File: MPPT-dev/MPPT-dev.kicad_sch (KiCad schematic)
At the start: 0 parts

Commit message: basic mppt
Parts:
- added U1: STM32L412KBUx, Package_DFN_QFN:QFN-32-1EP_5x5mm_P0.5mm_EP3.45x3.45mm, symbol MCU_ST_STM32L4:STM32L412KBUx
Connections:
- new net: U1.16 (VSS), U1.32 (VSS), U1.33 (VSS)
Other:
- added sheet MPPT (untitled.kicad_sch)
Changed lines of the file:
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@@
 	(generator_version "9.0")
 	(paper "A4")
+	(label "SDA"
+		(at 86.36 91.44 0)
+		(effects
+			(font
+				(size 1.27 1.27)
+			)
+			(justify left bottom)
+		)
+	)
+	(label "SCL"
+		(at 86.36 82.55 0)
+		(effects
+			(font
+				(size 1.27 1.27)
+			)
+			(justify left bottom)
+		)
+	)
+	(symbol
+		(lib_id "MCU_ST_STM32L4:STM32L412KBUx")
+		(at 69.85 92.71 0)
+		(unit 1)
+		(exclude_from_sim no)
+		(in_bom yes)
+		(on_board yes)
+		(dnp no)
+		(fields_autoplaced yes)
+		(property "Reference" "U1"
+			(at 71.9933 118.11 0)
+			(effects
+				(font
+					(size 1.27 1.27)
+				)
+				(justify left)
+			)
+		)
+		(property "Value" "STM32L412KBUx"
+			(at 71.9933 120.65 0)
+			(effects
+				(font
+					(size 1.27 1.27)
+				)
+				(justify left)
+			)
+		)
+		(property "Footprint" "Package_DFN_QFN:QFN-32-1EP_5x5mm_P0.5mm_EP3.45x3.45mm"
+			(at 59.69 115.57 0)
+			(effects
+				(font
+					(size 1.27 1.27)
+				)
+				(justify right)
+				(hide yes)
+			)
+		)
+		(property "Datasheet" "https://www.st.com/resource/en/datasheet/stm32l412kb.pdf"
+			(at 69.85 92.71 0)
+			(effects
+				(font
+					(size 1.27 1.27)
+				)
+				(hide yes)
+			)
+		)
+		(property "Description" "STMicroelectronics Arm Cortex-M4 MCU, 128KB flash, 40KB RAM, 80 MHz, 1.71-3.6V, 26 GPIO, UFQFPN32"
+			(at 69.85 92.71 0)
+			(effects
+				(font
+					(size 1.27 1.27)
+				)
+				(hide yes)
+			)
+		)
+		(pin "28"
+		)
+		(pin "5"
+		)
+		(pin "2"
+		)
+		(pin "15"
+		)
+		(pin "4"
+		)
+		(pin "21"
+		)
+		(pin "3"
+		)
+		(pin "31"
+		)
+		(pin "30"
+		)
+		(pin "9"
+		)
+		(pin "33"
+		)
+		(pin "27"
+		)
+		(pin "11"
+		)
+		(pin "13"
+		)
+		(pin "17"
+		)
+		(pin "25"
+		)
+		(pin "23"
+		)
+		(pin "24"
+		)
+		(pin "12"
+		)
+		(pin "18"
+		)
+		(pin "22"
+		)
+		(pin "19"
+		)
+		(pin "20"
+		)
+		(pin "29"
+		)
+		(pin "7"
+		)
+		(pin "16"
+		)
+		(pin "14"
+		)
+		(pin "32"
+		)
+		(pin "1"
+		)
+		(pin "8"
+		)
+		(pin "26"
+		)
+		(pin "6"
+		)
+		(pin "10"
+		)
+		(instances
+			(project ""
+				(path "/3a9896a7-b181-4cc9-9e66-236aedac8a9d"
+					(reference "U1")
+					(unit 1)
+				)
+			)
+		)
+	)
+	(sheet
+		(at 128.27 63.5)
+		(size 35.56 55.88)
+		(exclude_from_sim no)
+		(in_bom yes)
+		(on_board yes)
+		(dnp no)
+		(fields_autoplaced yes)
+		(stroke
+			(width 0.1524)
+			(type solid)
+		)
+		(fill
+			(color 0 0 0 0.0000)
+		)
+		(property "Sheetname" "MPPT"
+			(at 128.27 62.7884 0)
+			(effects
+				(font
+					(size 1.27 1.27)
+				)
+				(justify left bottom)
+			)
+		)
+		(property "Sheetfile" "untitled.kicad_sch"
+			(at 128.27 119.9646 0)
+			(effects
+				(font
+					(size 1.27 1.27)
+				)
+				(justify left top)
+			)
+		)
+		(instances
+			(project "MPPT-dev"
+				(path "/3a9896a7-b181-4cc9-9e66-236aedac8a9d"
+					(page "2")
+				)
+			)
+		)
+	)
 	(sheet_instances
 		(path "/"

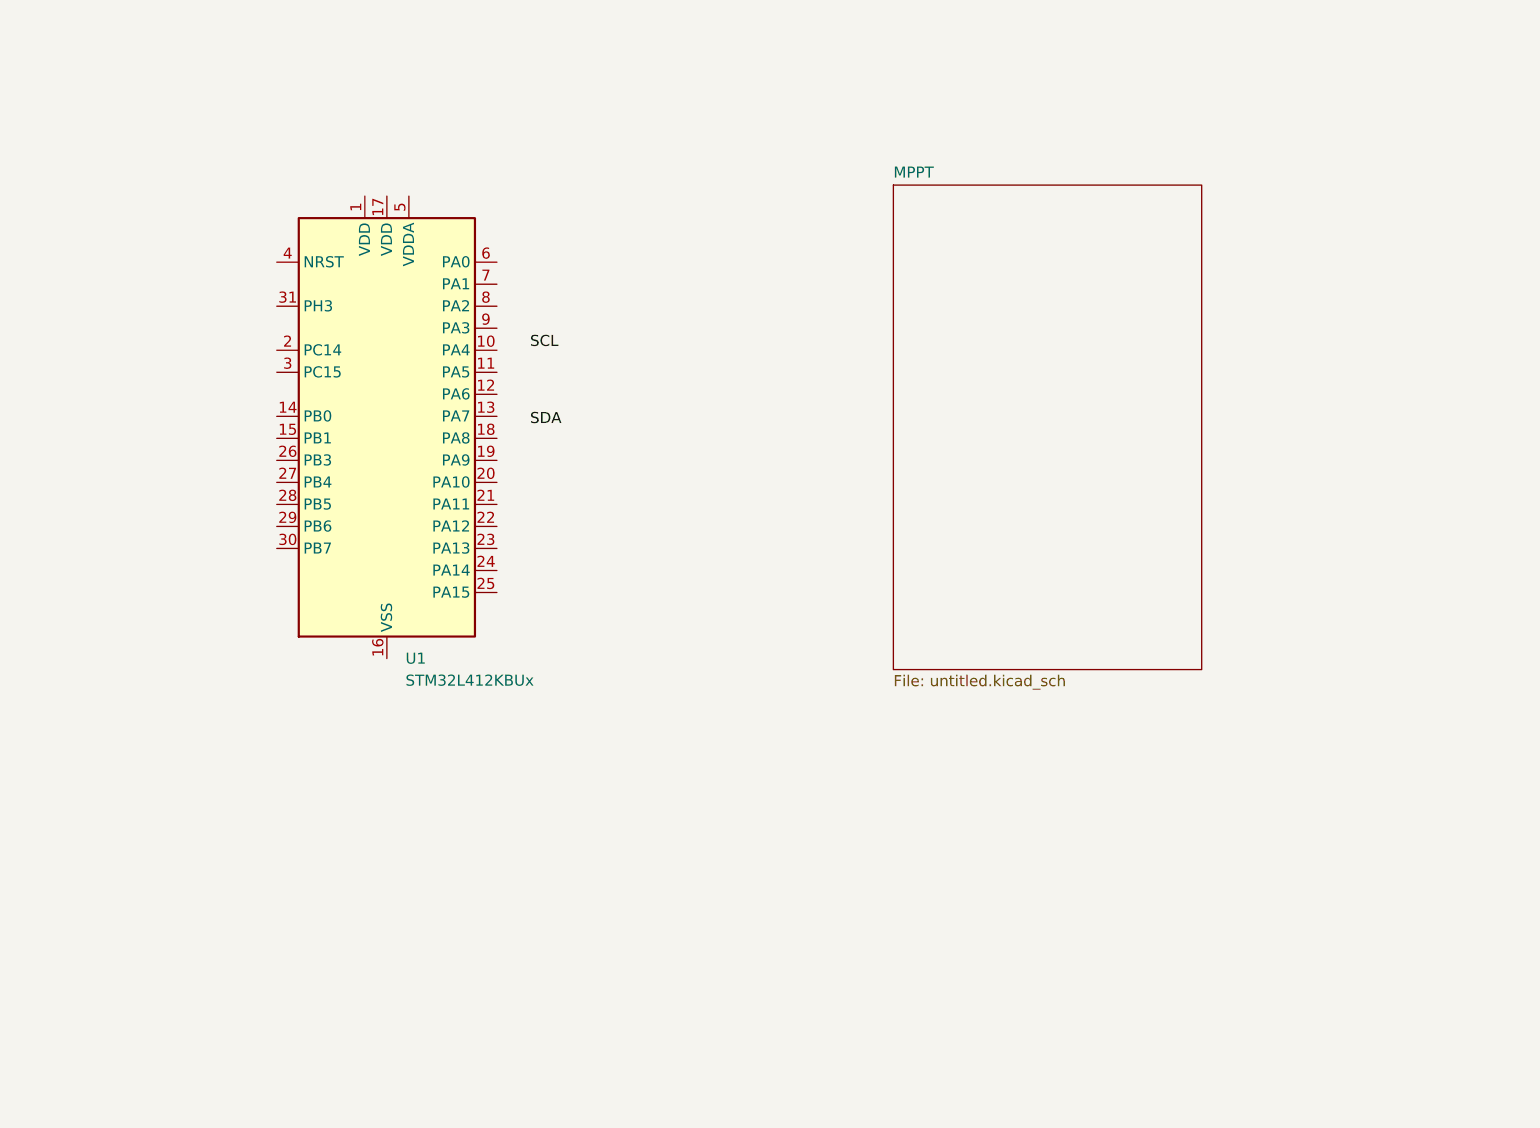
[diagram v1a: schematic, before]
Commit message: usb connector
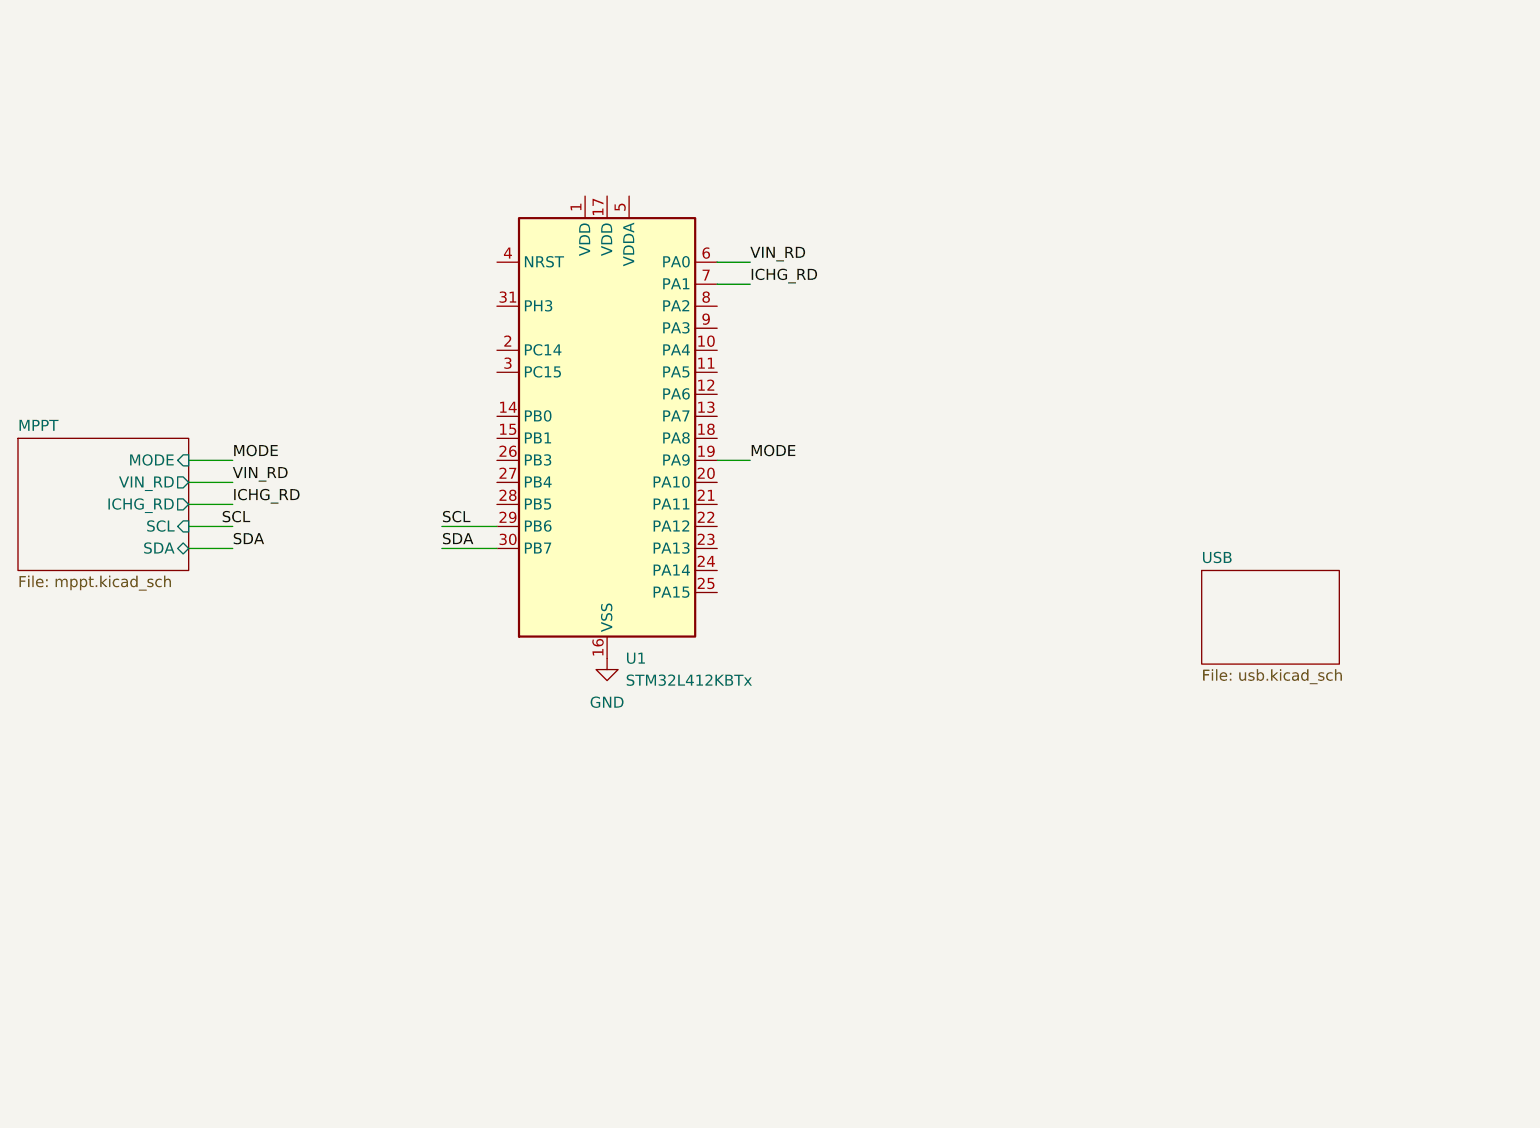
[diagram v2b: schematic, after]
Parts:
- removed U1: STM32L412KBUx, Package_DFN_QFN:QFN-32-1EP_5x5mm_P0.5mm_EP3.45x3.45mm, symbol MCU_ST_STM32L4:STM32L412KBUx
- added U1: STM32L412KBTx, Package_QFP:LQFP-32_7x7mm_P0.8mm, symbol MCU_ST_STM32L4:STM32L412KBTx
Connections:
- net SCL: now also U1.29 (PB6)
- net SDA: now also U1.30 (PB7)
- new net GND: U1.16 (VSS), U1.32 (VSS)
- new net ICHG_RD: U1.7 (PA1)
- new net MODE: U1.19 (PA9)
- new net VIN_RD: U1.6 (PA0)
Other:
- added sheet USB (usb.kicad_sch)
- sheet MPPT: file untitled.kicad_sch -> mppt.kicad_sch
- sheet MPPT ports: added ICHG_RD, MODE, SCL, SDA, VIN_RD; removed none

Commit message: initial layout
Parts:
- removed U1: STM32L412KBTx, Package_QFP:LQFP-32_7x7mm_P0.8mm, symbol MCU_ST_STM32L4:STM32L412KBTx
- added J1: 200528-0100, Argus-Connectors:Molex_200528-0100_1x10-1MP_P1.00mm_Horizontal, symbol Connector_Generic_MountingPin:Conn_01x10_MountingPin
- added J13: 282834-6, Connector_PinHeader_2.54mm:PinHeader_1x06_P2.54mm_Horizontal, symbol Connector_Generic:Conn_01x06
- added J2: Conn_01x02, Connector_PinHeader_2.54mm:PinHeader_1x02_P2.54mm_Horizontal, symbol Connector_Generic:Conn_01x02
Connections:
- net GND: now also J1.4 (Pin_4), J1.5 (Pin_5), J1.6 (Pin_6), J1.7 (Pin_7), J1.MP (MountPin), J13.6 (Pin_6), J2.1 (Pin_1)
- net ICHG_RD: now also J13.3 (Pin_3)
- net MODE: now also J13.1 (Pin_1)
- net SCL: now also J13.5 (Pin_5)
- net SDA: now also J13.4 (Pin_4)
- net VIN_RD: now also J13.2 (Pin_2)
- new net BATTERY: J2.2 (Pin_2)
- new net D_VSOLAR1: J1.1 (Pin_1), J1.2 (Pin_2), J1.3 (Pin_3)
- no-connect marks 0 -> 3
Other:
- removed sheet USB
- sheet MPPT ports: added BATTERY, SOLAR; removed none

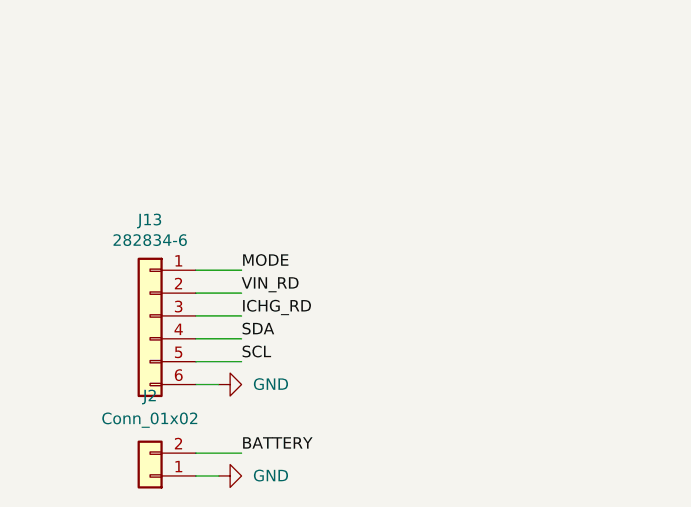
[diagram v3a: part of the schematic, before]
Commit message: 1 mppt layout
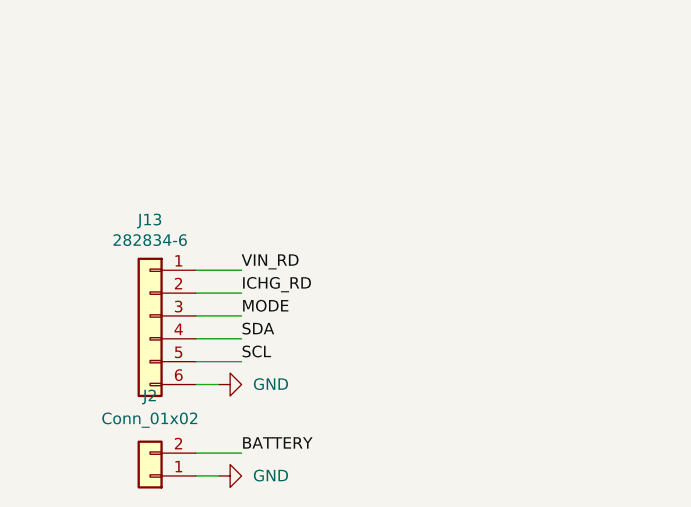
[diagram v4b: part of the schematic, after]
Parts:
- J13: footprint Connector_PinHeader_2.54mm:PinHeader_1x06_P2.54mm_Horizontal -> Connector_PinHeader_2.54mm:PinHeader_1x06_P2.54mm_Vertical
- J2: footprint Connector_PinHeader_2.54mm:PinHeader_1x02_P2.54mm_Horizontal -> Connector_PinHeader_2.54mm:PinHeader_1x02_P2.54mm_Vertical
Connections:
- net ICHG_RD: now also J13.2 (Pin_2); no longer J13.3 (Pin_3)
- net MODE: now also J13.3 (Pin_3); no longer J13.1 (Pin_1)
- net VIN_RD: now also J13.1 (Pin_1); no longer J13.2 (Pin_2)
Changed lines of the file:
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@@
 		)
 	)
-	(label "MODE"
+	(label "VIN_RD"
 		(at 52.07 146.05 0)
 		(effects
@@
 		)
 	)
-	(label "VIN_RD"
+	(label "ICHG_RD"
 		(at 52.07 148.59 0)
 		(effects
@@
 		)
 	)
-	(label "ICHG_RD"
+	(label "MODE"
 		(at 52.07 151.13 0)
 		(effects
@@
 			)
 		)
-		(property "Footprint" "Connector_PinHeader_2.54mm:PinHeader_1x02_P2.54mm_Horizontal"
+		(property "Footprint" "Connector_PinHeader_2.54mm:PinHeader_1x02_P2.54mm_Vertical"
 			(at 41.91 168.91 0)
 			(effects
@@
 			)
 		)
-		(property "Footprint" "Connector_PinHeader_2.54mm:PinHeader_1x06_P2.54mm_Horizontal"
+		(property "Footprint" "Connector_PinHeader_2.54mm:PinHeader_1x06_P2.54mm_Vertical"
 			(at 41.91 151.13 0)
 			(effects

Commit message: Board review
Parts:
- J1: footprint Argus-Connectors:Molex_200528-0100_1x10-1MP_P1.00mm_Horizontal -> footprints:Molex_200528-0100_1x10-1MP_P1.00mm_Horizontal
- J3: renamed from J13; value 282834-6 -> Conn_01x07; footprint Connector_PinHeader_2.54mm:PinHeader_1x06_P2.54mm_Vertical -> Connector_PinHeader_2.54mm:PinHeader_1x07_P2.54mm_Vertical; symbol Connector_Generic:Conn_01x06 -> Connector_Generic:Conn_01x07
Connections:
- net GND: now also J3.7 (Pin_7); no longer J3.6 (Pin_6)
- net ICHG_RD: now also J3.5 (Pin_5); no longer J3.2 (Pin_2)
- net MODE: now also J3.6 (Pin_6); no longer J3.3 (Pin_3)
- net SCL: now also J3.2 (Pin_2); no longer J3.5 (Pin_5)
- net SDA: now also J3.3 (Pin_3); no longer J3.4 (Pin_4)
- net VIN_RD: now also J3.4 (Pin_4); no longer J3.1 (Pin_1)
- new net +3V3: J3.1 (Pin_1)
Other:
- moved on the sheet: J1, J2
